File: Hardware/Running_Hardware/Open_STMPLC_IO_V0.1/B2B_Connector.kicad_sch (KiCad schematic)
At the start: 41 parts, among them J1 Screw_Terminal_01x10, J2 Screw_Terminal_01x06, J39 10144517-041802LF, J41 10144517-041802LF, J42 10144517-041802LF, J43 Screw_Terminal_01x02, J9 DE9_Pins, Q5 AOD407, Q6 AOD407, Q7 MMBT5401

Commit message: IO board layout
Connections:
- net Ethernet_Activity_LED is gone; now on net NET_MODE_LED: D104.1 (K)
- net Ethernet_Link_LED is gone; now on net NET_STATUS_LED: D103.1 (K)
- net Internet_Status_LED is gone; now on net GSM_STATUS_LED: D105.1 (K)
- net POWER_LED is gone; now on net GND: D100.1 (K)
- net +24V: no longer J41.7 (Pin_7)
- net +3V3: no longer J41.8 (Pin_8)
- net 3V3_ISO: now also J42.29 (Pin_29); no longer J42.37 (Pin_37)
- net AB+: now also J42.36 (Pin_36); no longer J42.35 (Pin_35)
- net AB-: now also J42.34 (Pin_34); no longer J42.33 (Pin_33)
- net ANALOG_IN_CS: now also J41.28 (Pin_28)
- net ANALOG_IN_DIN: now also J41.29 (Pin_29)
- net ANALOG_IN_DOUT: now also J41.27 (Pin_27)
- net ANALOG_IN_ERROR: now also J41.30 (Pin_30)
- net ANALOG_IN_SCLK: now also J41.31 (Pin_31)
- net AOUT_EFCM_1: now also J39.15 (Pin_15)
- net AOUT_EFCM_2: now also J39.16 (Pin_16)
- net AOUT_EFLD_1: now also J39.13 (Pin_13)
- net AOUT_EFLD_2: now also J39.14 (Pin_14)
- net AOUT_EFOT_1: now also J39.11 (Pin_11)
- net AOUT_EFOT_2: now also J39.12 (Pin_12)
- net AOUT_M1_1: now also J39.5 (Pin_5)
- net AOUT_M1_2: now also J39.6 (Pin_6)
- net AOUT_M2_1: now also J39.7 (Pin_7)
- net AOUT_M2_2: now also J39.8 (Pin_8)
- net AOUT_VIN_1: now also J39.3 (Pin_3)
- net AOUT_VIN_2: now also J39.4 (Pin_4)
- net AOUT_~{OD}_1: now also J39.9 (Pin_9)
- net AOUT_~{OD}_2: now also J39.10 (Pin_10)
- net DIG_HS_IMON_1: now also J41.9 (Pin_9)
- net DIG_HS_IMON_2: now also J41.10 (Pin_10)
- net DIG_HS_IMON_3: now also J41.23 (Pin_23)
- net DIG_HS_IMON_4: now also J41.22 (Pin_22)
- net DIG_HS_OUT_1: now also J41.13 (Pin_13)
- net DIG_HS_OUT_2: now also J41.14 (Pin_14)
- net DIG_HS_OUT_3: now also J41.17 (Pin_17)
- net DIG_HS_OUT_4: now also J41.18 (Pin_18)
- net DIG_HS_~{FAULT}_1: now also J41.11 (Pin_11)
- net DIG_HS_~{FAULT}_2: now also J41.12 (Pin_12)
- net DIG_HS_~{FAULT}_3: now also J41.21 (Pin_21)
- net DIG_HS_~{FAULT}_4: now also J41.24 (Pin_24)
- net DIG_HS_~{SHDN}_1: now also J41.7 (Pin_7)
- net DIG_HS_~{SHDN}_2: now also J41.8 (Pin_8)
- net DIG_HS_~{SHDN}_3: now also J41.19 (Pin_19)
- net DIG_HS_~{SHDN}_4: now also J41.20 (Pin_20)
- net DIG_IN_1: now also J39.37 (Pin_37)
- net DIG_IN_10: now also J41.33 (Pin_33)
- net DIG_IN_11: now also J41.35 (Pin_35)
- net DIG_IN_12: now also J41.37 (Pin_37)
- net DIG_IN_2: now also J39.35 (Pin_35)
- net DIG_IN_3: now also J39.33 (Pin_33)
- net DIG_IN_4: now also J39.31 (Pin_31)
- net DIG_IN_5: now also J39.29 (Pin_29)
- net DIG_IN_6: now also J39.27 (Pin_27)
- net DIG_IN_7: now also J41.34 (Pin_34)
- net DIG_IN_8: now also J41.36 (Pin_36)
- net DIG_IN_9: now also J41.38 (Pin_38)
- net DIG_OUT_1: now also J42.24 (Pin_24)
- net DIG_OUT_2: now also J42.23 (Pin_23)
- net DIG_OUT_3: now also J42.22 (Pin_22)
- net DIG_OUT_4: now also J42.21 (Pin_21)
- net DIG_OUT_5: now also J42.14 (Pin_14)
- net DIG_OUT_6: now also J42.13 (Pin_13)
- net DIG_OUT_7: now also J42.7 (Pin_7)
- net DIG_OUT_8: now also J42.8 (Pin_8)
- net DIG_OUT_DIAG_1: now also J42.26 (Pin_26)
- net DIG_OUT_DIAG_2: now also J42.25 (Pin_25)
- net DIG_OUT_DIAG_3: now also J42.20 (Pin_20)
- net DIG_OUT_DIAG_4: now also J42.19 (Pin_19)
- net DIG_OUT_DIAG_5: now also J42.12 (Pin_12)
- net DIG_OUT_DIAG_6: now also J42.11 (Pin_11)
- net DIG_OUT_DIAG_7: now also J42.5 (Pin_5)
- net DIG_OUT_DIAG_8: now also J42.6 (Pin_6)
- net DIG_OUT_~{FAULT}_1: now also J42.28 (Pin_28)
- net DIG_OUT_~{FAULT}_2: now also J42.27 (Pin_27)
- net DIG_OUT_~{FAULT}_3: now also J42.18 (Pin_18)
- net DIG_OUT_~{FAULT}_4: now also J42.17 (Pin_17)
- net DIG_OUT_~{FAULT}_5: now also J42.10 (Pin_10)
- net DIG_OUT_~{FAULT}_6: now also J42.9 (Pin_9)
- net DIG_OUT_~{FAULT}_7: now also J42.3 (Pin_3)
- net DIG_OUT_~{FAULT}_8: now also J42.4 (Pin_4)
- net FAULT_LED: now also J42.16 (Pin_16)
- net GND: now also J41.15 (Pin_15), J41.16 (Pin_16), J41.25 (Pin_25), J41.26 (Pin_26), J41.32 (Pin_32), J42.30 (Pin_30)
- net GND_MODBUS: now also J42.31 (Pin_31), J42.32 (Pin_32), J42.37 (Pin_37)
- net RTD_~{CS}_1: now also J39.19 (Pin_19)
- net RTD_~{CS}_2: now also J39.21 (Pin_21)
- net RTD_~{DRDY}_1: now also J39.22 (Pin_22)
- net RTD_~{DRDY}_2: now also J39.26 (Pin_26)
- net RUN_LED: now also J42.15 (Pin_15)
- net TEMP_MISO: now also J39.17 (Pin_17)
- net TEMP_MOSI: now also J39.25 (Pin_25)
- net TEMP_SCLK: now also J39.23 (Pin_23)
- net THRM_~{CS}: now also J39.18 (Pin_18)
- net THRM_~{DRDY}: now also J39.24 (Pin_24)
- net THRM_~{FAULT}: now also J39.20 (Pin_20)
- net YZ+: now also J42.35 (Pin_35); no longer J42.34 (Pin_34)
- net YZ-: now also J42.33 (Pin_33); no longer J42.36 (Pin_36)
- net GSM_STATUS_LED: now reaches J39.28 (Pin_28)
- net NET_MODE_LED: now reaches J39.30 (Pin_30)
- net NET_STATUS_LED: now reaches J39.32 (Pin_32)
- no-connect marks 2 -> 5
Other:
- note added: "B2B CONNECTORS"
- note added: "MODBUS CONNECTOR"
- note added: "POWER INPUT"
- moved on the sheet: C46, C47, C48, C50, C51, C89, C90, D100, D101, D102, D103, D104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

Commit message: Main PCB changes
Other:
- note added: "COMMON TERMINALS"
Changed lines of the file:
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@@
 	(rectangle
 		(start 13.97 13.97)
-		(end 281.94 87.63)
+		(end 212.09 87.63)
 		(stroke
 			(width 0)
@@
 		)
 	)
+	(rectangle
+		(start 215.9 13.97)
+		(end 281.94 87.63)
+		(stroke
+			(width 0)
+			(type default)
+		)
+		(fill
+			(type none)
+		)
+	)
+	(text "COMMON TERMINALS"
+		(exclude_from_sim no)
+		(at 216.662 17.018 0)
+		(effects
+			(font
+				(size 3 3)
+				(thickness 0.6)
+				(bold yes)
+			)
+			(justify left)
+		)
+	)
 	(text "POWER INPUT"
 		(exclude_from_sim no)
@@
 		(effects
 			(font
-				(size 1.27 1.27)
+				(size 1 1)
 			)
 			(justify right bottom)
@@
 		(effects
 			(font
-				(size 1.27 1.27)
+				(size 1 1)
 			)
 			(justify left bottom)
@@
 		(effects
 			(font
-				(size 1.27 1.27)
+				(size 1 1)
 			)
 			(justify left bottom)
@@
 		(effects
 			(font
-				(size 1.27 1.27)
+				(size 1 1)
 			)
 			(justify right bottom)
@@
 		(effects
 			(font
-				(size 1.27 1.27)
+				(size 1 1)
 			)
 			(justify right bottom)
@@
 		(effects
 			(font
-				(size 1.27 1.27)
+				(size 1 1)
 			)
 			(justify left bottom)
@@
 		(effects
 			(font
-				(size 1.27 1.27)
+				(size 1 1)
 			)
 			(justify left bottom)
@@
 		(effects
 			(font
-				(size 1.27 1.27)
+				(size 1 1)
 			)
 			(justify left bottom)
@@
 		(effects
 			(font
-				(size 1.27 1.27)
+				(size 1 1)
 			)
 			(justify right bottom)
@@
 		(effects
 			(font
-				(size 1.27 1.27)
+				(size 1 1)
 			)
 			(justify left bottom)
@@
 		(effects
 			(font
-				(size 1.27 1.27)
+				(size 1 1)
 			)
 			(justify left bottom)
@@
 		(effects
 			(font
-				(size 1.27 1.27)
+				(size 1 1)
 			)
 			(justify left bottom)
@@
 		(effects
 			(font
-				(size 1.27 1.27)
+				(size 1 1)
 			)
 			(justify right bottom)
@@
 		(effects
 			(font
-				(size 1.27 1.27)
+				(size 1 1)
 			)
 			(justify right bottom)
@@
 		(effects
 			(font
-				(size 1.27 1.27)
+				(size 1 1)
 			)
 			(justify left bottom)
@@
 		(effects
 			(font
-				(size 1.27 1.27)
+				(size 1 1)
 			)
 			(justify left bottom)
@@
 		(effects
 			(font
-				(size 1.27 1.27)
+				(size 1 1)
 			)
 			(justify left bottom)
@@
 		(effects
 			(font
-				(size 1.27 1.27)
+				(size 1 1)
 			)
 			(justify left bottom)
@@
 		(effects
 			(font
-				(size 1.27 1.27)
+				(size 1 1)
 			)
 			(justify left bottom)
@@
 		(effects
 			(font
-				(size 1.27 1.27)
+				(size 1 1)
 			)
 			(justify left bottom)
@@
 			(effects
 				(font
-					(size 1.27 1.27)
+					(size 1 1)
 				)
 				(justify right)
@@
 			(effects
 				(font
-					(size 1.27 1.27)
+					(size 1 1)
 				)
 				(justify right)
@@
 			(effects
 				(font
-					(size 1.27 1.27)
+					(size 1 1)
 				)
 				(justify right)
@@
 			(effects
 				(font
-					(size 1.27 1.27)
+					(size 1 1)
 				)
 				(justify right)
@@
 			(effects
 				(font
-					(size 1.27 1.27)
+					(size 1 1)
 				)
 				(justify right)
@@
 			(effects
 				(font
-					(size 1.27 1.27)
+					(size 1 1)
 				)
 				(justify right)
@@
 			(effects
 				(font
-					(size 1.27 1.27)
+					(size 1 1)
 				)
 				(justify right)
@@
 			(effects
 				(font
-					(size 1.27 1.27)
+					(size 1 1)
 				)
 				(justify right)
@@
 			(effects
 				(font
-					(size 1.27 1.27)
+					(size 1 1)
 				)
 				(justify right)
@@
 			(effects
 				(font
-					(size 1.27 1.27)
+					(size 1 1)
 				)
 				(justify right)
@@
 			(effects
 				(font
-					(size 1.27 1.27)
+					(size 1 1)
 				)
 				(justify right)
@@
 			(effects
 				(font
-					(size 1.27 1.27)
+					(size 1 1)
 				)
 				(justify right)

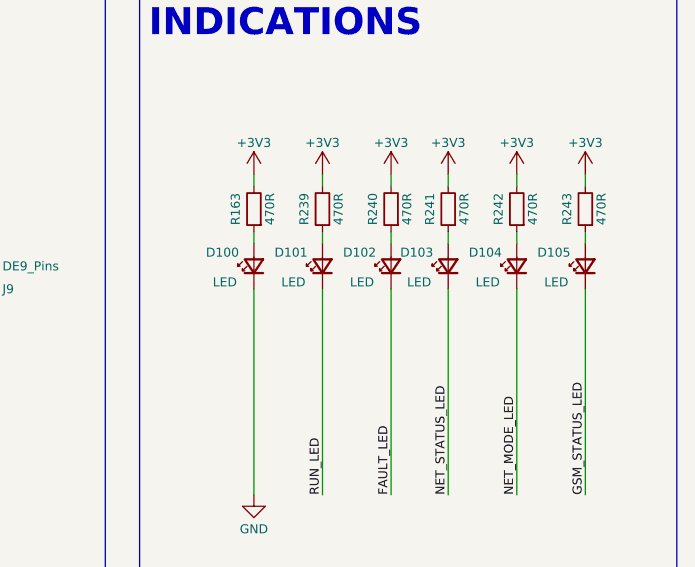
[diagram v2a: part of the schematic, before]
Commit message: Schematic updates
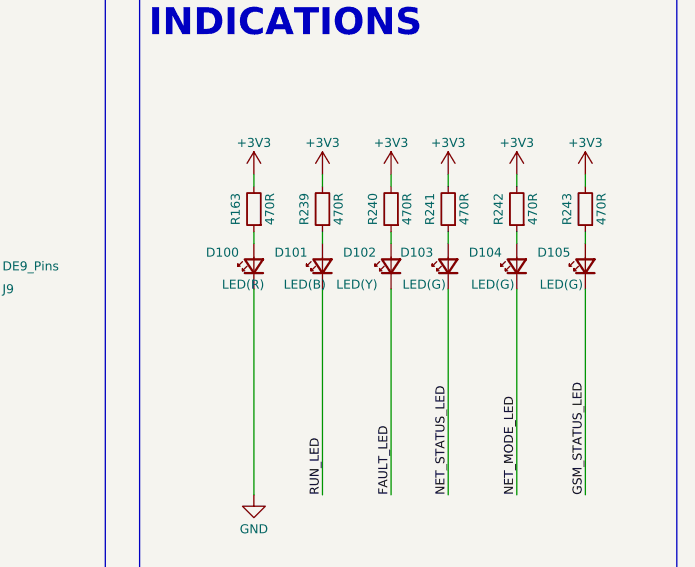
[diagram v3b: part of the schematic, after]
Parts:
- D100: value LED -> LED(R)
- D101: value LED -> LED(B)
- D102: value LED -> LED(Y)
- D103, D104, D105: value LED -> LED(G)
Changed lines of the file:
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@@
 			)
 		)
-		(property "Value" "LED"
-			(at 259.588 123.698 90)
+		(property "Value" "LED(G)"
+			(at 259.08 123.952 90)
 			(effects
 				(font
@@
 			)
 		)
-		(property "Value" "LED"
-			(at 230.378 123.698 90)
+		(property "Value" "LED(R)"
+			(at 231.394 123.952 90)
 			(effects
 				(font
@@
 			)
 		)
-		(property "Value" "LED"
-			(at 251.968 123.698 90)
+		(property "Value" "LED(G)"
+			(at 251.46 123.952 90)
 			(effects
 				(font
@@
 			)
 		)
-		(property "Value" "LED"
-			(at 245.618 123.698 90)
+		(property "Value" "LED(Y)"
+			(at 244.094 123.952 90)
 			(effects
 				(font
@@
 			)
 		)
-		(property "Value" "LED"
-			(at 237.998 123.698 90)
+		(property "Value" "LED(B)"
+			(at 238.252 123.952 90)
 			(effects
 				(font
@@
 			)
 		)
-		(property "Value" "LED"
-			(at 267.208 123.698 90)
+		(property "Value" "LED(G)"
+			(at 266.7 123.952 90)
 			(effects
 				(font

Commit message: Silkscreen and DRC
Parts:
- J39, J41, J42: value 10144517-041802LF -> 10144517-042802LF
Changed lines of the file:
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@@
 			)
 		)
-		(property "Value" "10144517-041802LF"
+		(property "Value" "10144517-042802LF"
 			(at 184.15 24.13 0)
 			(effects
@@
 			)
 		)
-		(property "Value" "10144517-041802LF"
+		(property "Value" "10144517-042802LF"
 			(at 114.3 24.13 0)
 			(effects
@@
 			)
 		)
-		(property "Value" "10144517-041802LF"
+		(property "Value" "10144517-042802LF"
 			(at 53.34 24.13 0)
 			(effects

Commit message: Gerber generation v0.1
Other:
- company: (none) -> Thingslista Automation LLP
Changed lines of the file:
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@@
 	(title_block
 		(title "Open_STMPLC_IO")
-		(date "2026-05-23")
+		(date "2026-06-03")
 		(rev "0.1")
+		(company "Thingslista Automation LLP")
 	)
 	(rectangle
